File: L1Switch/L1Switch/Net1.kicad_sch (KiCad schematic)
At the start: 66 parts, among them J8 Conn_01x07_Male, U9 VSC8658

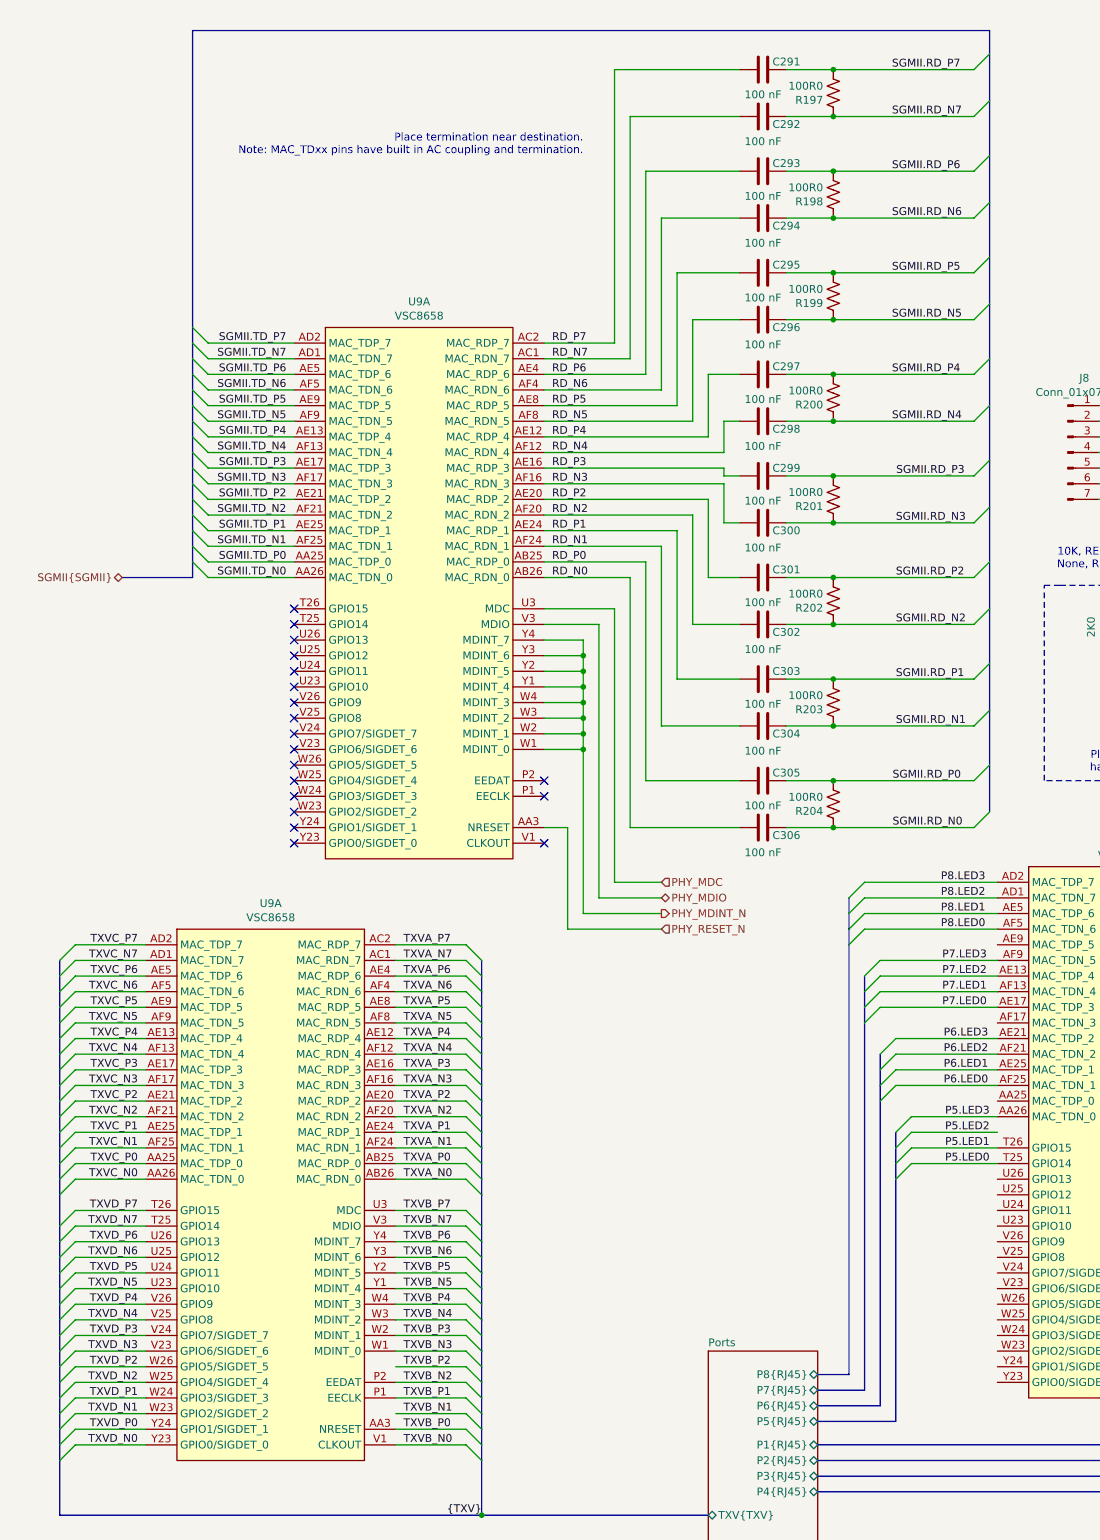
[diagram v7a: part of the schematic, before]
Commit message: Finish length matching. Move the layout onto a larger sheet to fit.
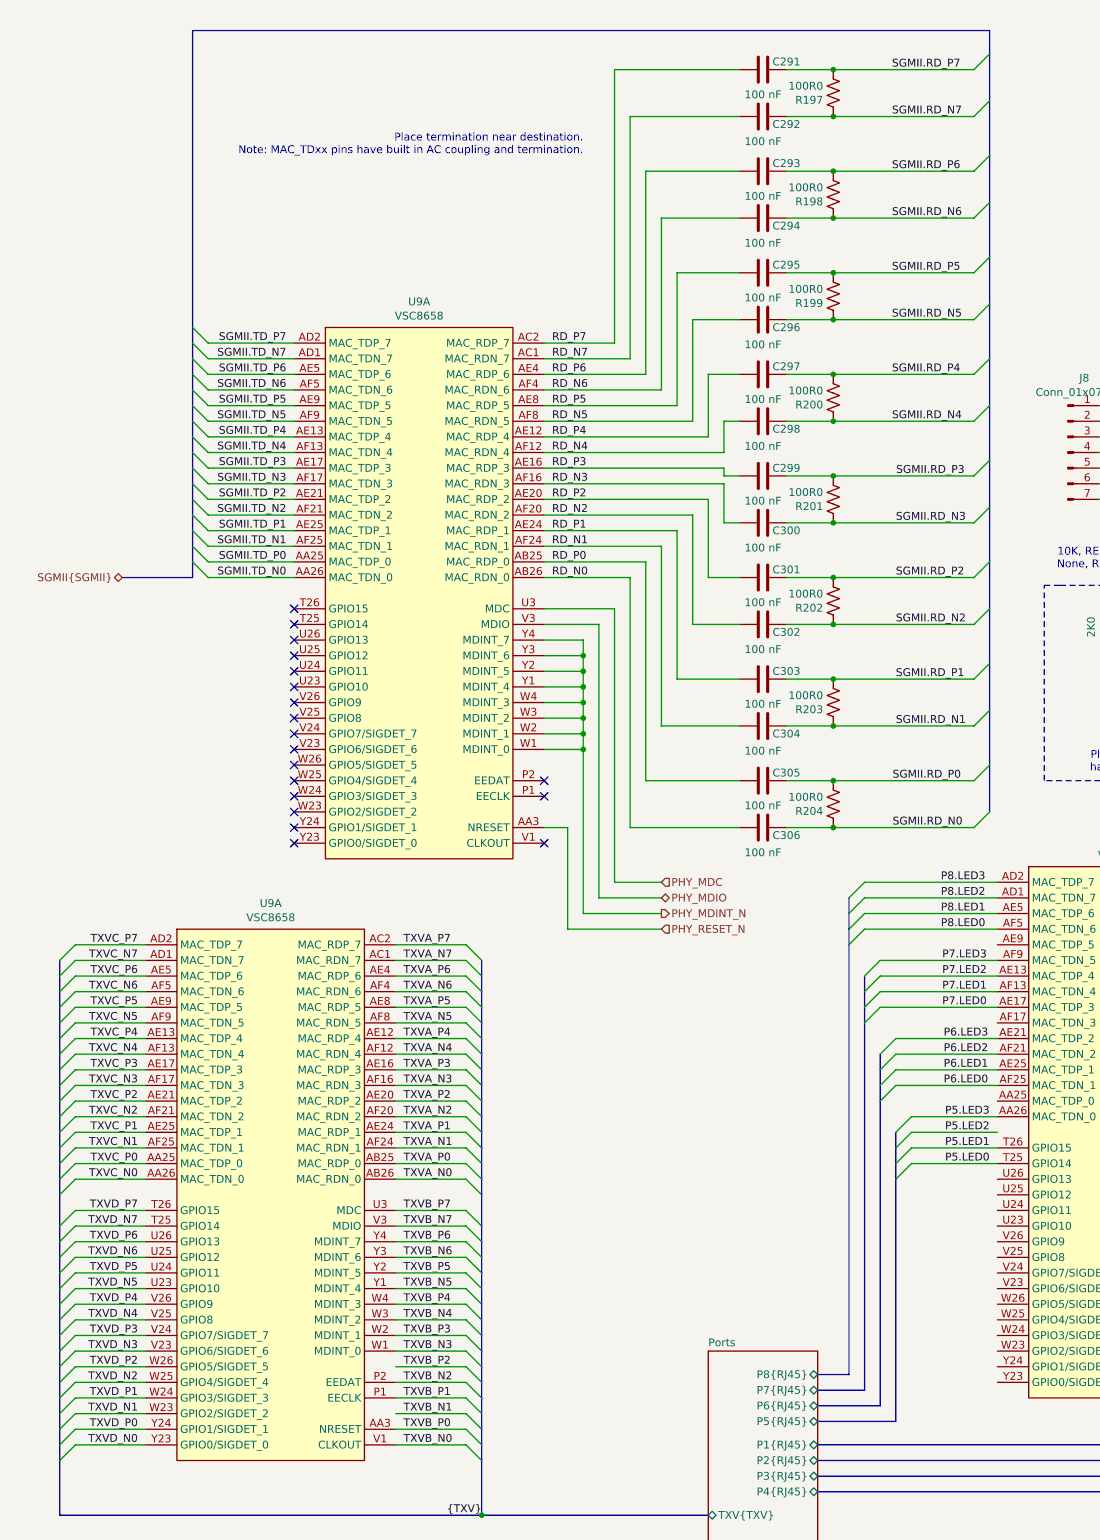
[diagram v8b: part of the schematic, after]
